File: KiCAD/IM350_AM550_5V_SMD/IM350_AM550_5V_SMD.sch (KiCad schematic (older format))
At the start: 10 parts, among them J5 USB_B_Micro_Power, J7 RJ12, P3 0R, P4 0R, SW1 Pairing, U1 MCP1700-3302E_SOT23, U2 ESP-12F

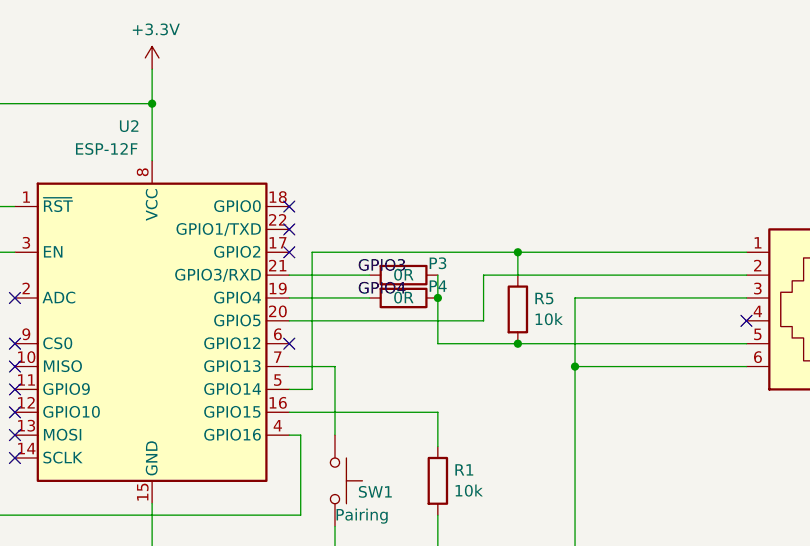
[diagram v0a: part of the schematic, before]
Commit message: Website handleSettings bugfix
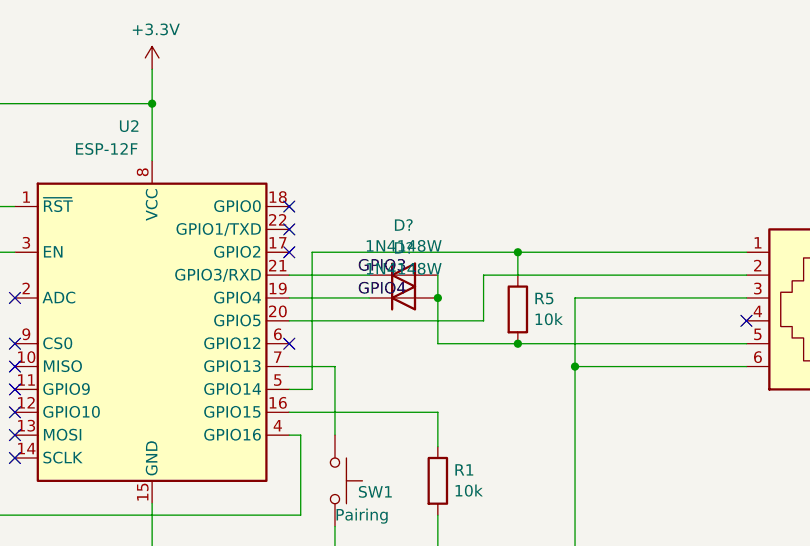
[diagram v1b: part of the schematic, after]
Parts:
- removed P3, P4: 0R, Resistor_SMD:R_0402_1005Metric_Pad0.72x0.64mm_HandSolder, symbol Device:R
- added D? (x2): 1N4148W, Diode_SMD:D_SOD-123, symbol Diode:1N4148W
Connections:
- net GPIO3: now also D?.1 (K)
- net GPIO4: now also D?.1 (K)
- net at J7.5, R5.2: now also D?.2 (A), D?.2 (A)
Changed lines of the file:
@@
 NoConn ~ 5450 3000
 NoConn ~ 5450 3100
-$Comp
-L Device:R P3
-U 1 1 606C9BA3
-P 7150 2300
-F 0 "P3" V 7100 2450 50  0000 C CNN
-F 1 "0R" V 7150 2300 50  0000 C CNN
-F 2 "Resistor_SMD:R_0402_1005Metric_Pad0.72x0.64mm_HandSolder" V 7080 2300 50  0001 C CNN
-F 3 "~" H 7150 2300 50  0001 C CNN
-	1    7150 2300
-	0    1    1    0
-$EndComp
 Connection ~ 7650 2600
 Wire Wire Line
@@
 	6650 2500 7500 2500
 Wire Wire Line
-	7300 2300 7300 2400
-Wire Wire Line
 	7300 2600 7650 2600
 Wire Wire Line
@@
 Wire Wire Line
 	3500 2500 4200 2500
-$Comp
-L Device:R P4
-U 1 1 60715416
-P 7150 2400
-F 0 "P4" V 7100 2550 50  0000 C CNN
-F 1 "0R" V 7150 2400 50  0000 C CNN
-F 2 "Resistor_SMD:R_0402_1005Metric_Pad0.72x0.64mm_HandSolder" V 7080 2400 50  0001 C CNN
-F 3 "~" H 7150 2400 50  0001 C CNN
-	1    7150 2400
-	0    1    1    0
-$EndComp
-Connection ~ 7300 2400
-Wire Wire Line
-	7300 2400 7300 2600
 Wire Wire Line
 	6650 2400 7000 2400
@@
 NoConn ~ 6650 2000
 NoConn ~ 6650 2100
+$Comp
+L Diode:1N4148W D?
+U 1 1 610C304B
+P 7150 2300
+F 0 "D?" H 7150 2517 50  0000 C CNN
+F 1 "1N4148W" H 7150 2426 50  0000 C CNN
+F 2 "Diode_SMD:D_SOD-123" H 7150 2125 50  0001 C CNN
+F 3 "https://www.vishay.com/docs/85748/1n4148w.pdf" H 7150 2300 50  0001 C CNN
+	1    7150 2300
+	1    0    0    -1
+$EndComp
+Wire Wire Line
+	7300 2300 7300 2400
+$Comp
+L Diode:1N4148W D?
+U 1 1 610C3C9E
+P 7150 2400
+F 0 "D?" H 7150 2617 50  0000 C CNN
+F 1 "1N4148W" H 7150 2526 50  0000 C CNN
+F 2 "Diode_SMD:D_SOD-123" H 7150 2225 50  0001 C CNN
+F 3 "https://www.vishay.com/docs/85748/1n4148w.pdf" H 7150 2400 50  0001 C CNN
+	1    7150 2400
+	1    0    0    -1
+$EndComp
+Connection ~ 7300 2400
+Wire Wire Line
+	7300 2400 7300 2600
 $EndSCHEMATC
